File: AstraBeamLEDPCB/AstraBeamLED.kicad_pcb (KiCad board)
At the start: 2 copper layers, 75 x 55 mm, 20 parts

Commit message: Cleanup
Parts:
- removed kibuzzard-67294CE8: G***, kibuzzard-67294CE8
- removed kibuzzard-67294ED0: G***, kibuzzard-67294ED0
- added kibuzzard-672E94DA: G***, kibuzzard-672E94DA, F.Cu at (117.8, 113.0)
- added kibuzzard-672E94E0: G***, kibuzzard-672E94E0, F.Cu at (181.5, 87.0)
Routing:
- net /Schematic/GREEN+: track 41.3 -> 39.9 mm
- net /Schematic/CY-: track 41.3 -> 39.9 mm
- net /Schematic/RED+: track 40.5 -> 39.9 mm
- net /Schematic/BLUE-: track 40.5 -> 39.9 mm

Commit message: fix font
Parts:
- added kibuzzard-678EC3F2: G***, kibuzzard-678EC3F2, F.Cu at (150.0, 88.5)

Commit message: Add 40W
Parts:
- removed kibuzzard-67294F39: G***, kibuzzard-67294F39
- added kibuzzard-678EC518: G***, kibuzzard-678EC518, F.Cu at (150.0, 117.5)

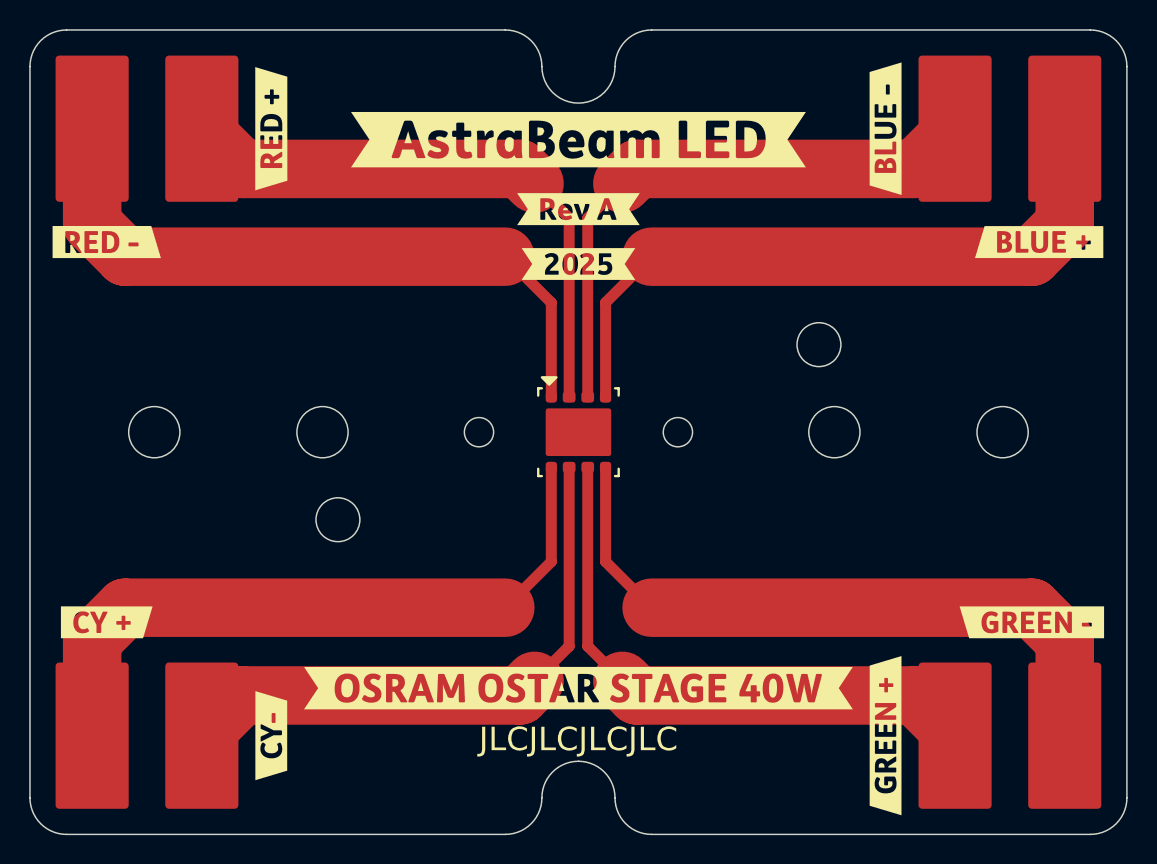
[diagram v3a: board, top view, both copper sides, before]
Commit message: Tweak mounting holes
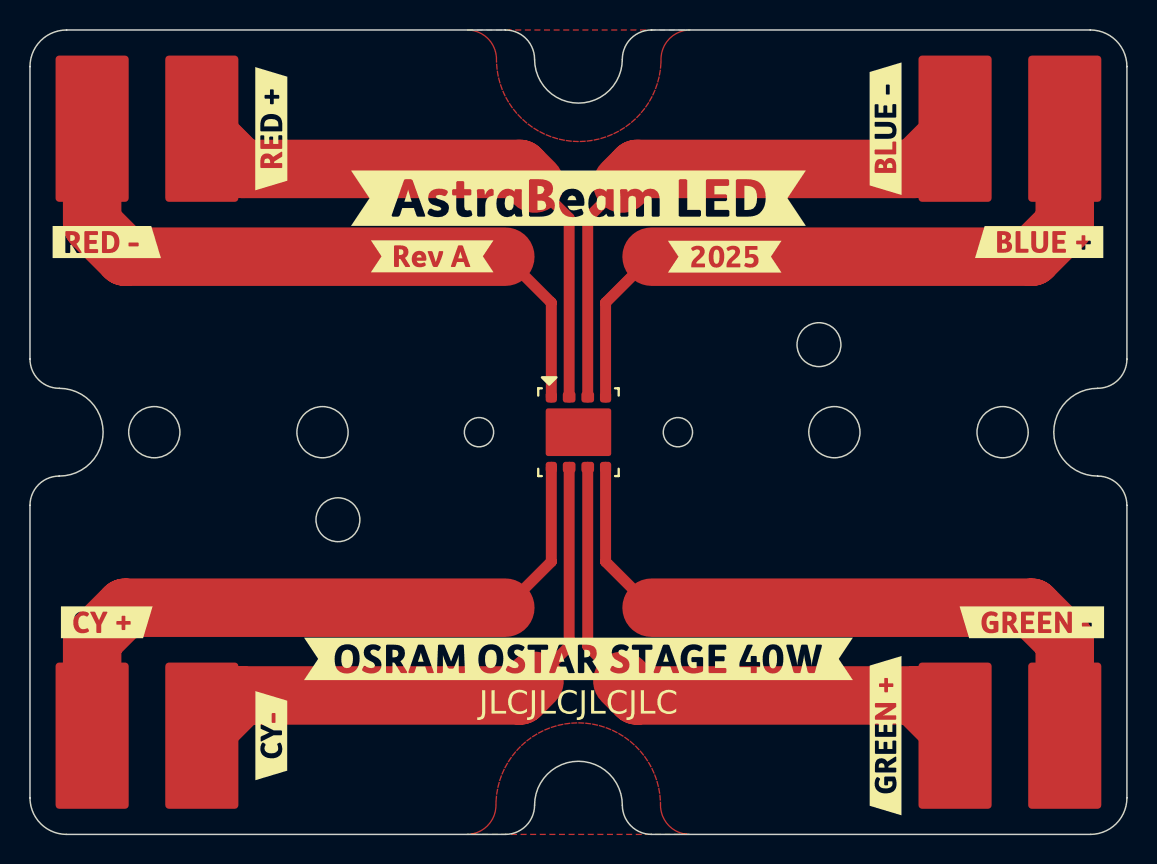
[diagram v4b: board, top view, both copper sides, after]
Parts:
- moved kibuzzard-67294BDE 10.5 mm to (140.0, 88.0)
- moved kibuzzard-678EC3F2 10.0 mm to (160.0, 88.0)
- moved kibuzzard-67294BF2 4.00 mm to (150.0, 84.0)
- moved kibuzzard-678EC518 2.00 mm to (150.0, 115.5)
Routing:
- added copper zone on F.Cu, net (none)
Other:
- outline, holes or cut-outs redrawn
